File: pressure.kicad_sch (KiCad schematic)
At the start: 9 parts, among them IC1 HSFPAR004A, U6 INA317IDGKR

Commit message: finish up routing and fix latching
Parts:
- R21, R27: footprint Resistor_SMD:R_0603_1608Metric -> Resistor_SMD:R_1206_3216Metric
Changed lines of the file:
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@@
 			)
 		)
-		(property "Footprint" "Resistor_SMD:R_0603_1608Metric"
+		(property "Footprint" "Resistor_SMD:R_1206_3216Metric"
 			(at 110.998 63.5 90)
 			(effects
@@
 			)
 		)
-		(property "Footprint" "Resistor_SMD:R_0603_1608Metric"
+		(property "Footprint" "Resistor_SMD:R_1206_3216Metric"
 			(at 88.392 76.2 90)
 			(effects

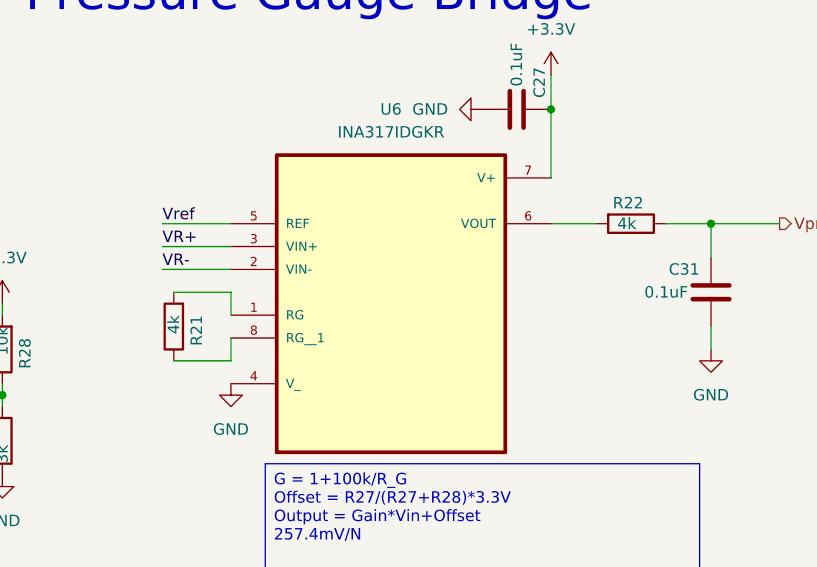
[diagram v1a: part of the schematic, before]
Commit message: replace some components for JLC order
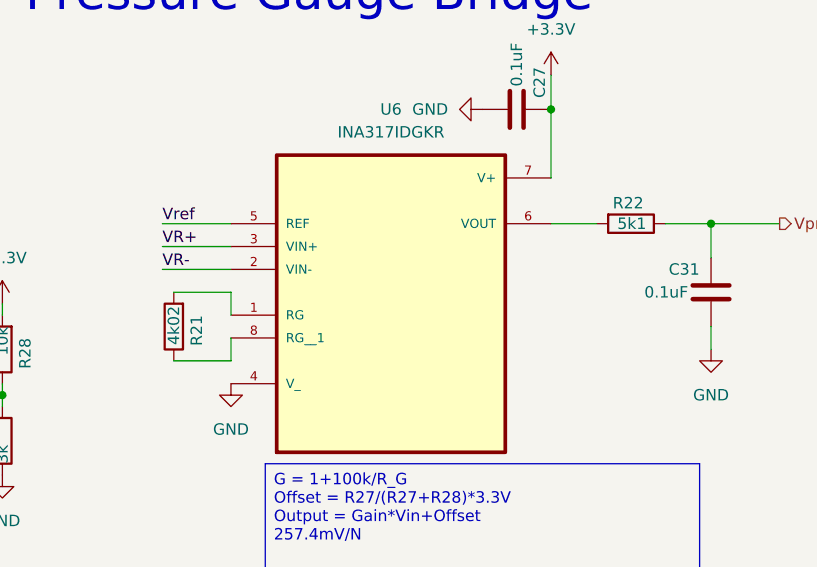
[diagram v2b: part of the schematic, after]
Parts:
- IC1: mpn (none) -> HSFPAR004A
- R21: value 4k -> 4k02; mpn CR0805-FX-1002ELF -> RC1206FR-074K02L
- R22: value 4k -> 5k1; mpn CR0805-FX-1002ELF -> (none)
- R27, R28: mpn CR0805-FX-1002ELF -> (none)
- U6: mpn (none) -> INA317IDGKR
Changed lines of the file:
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@@
 			)
 		)
-		(property "Value" "4k"
-			(at 109.22 62.23 90)
+		(property "Value" "4k02"
+			(at 109.22 61.214 90)
 			(effects
 				(font
@@
 			)
 		)
-		(property "mpn" "CR0805-FX-1002ELF "
+		(property "mpn" "RC1206FR-074K02L"
 			(at 109.22 63.5 0)
 			(effects
@@
 			)
 		)
-		(property "mpn" "CR0805-FX-1002ELF "
+		(property "mpn" ""
 			(at 90.17 76.2 0)
 			(effects
@@
 			)
 		)
+		(property "mpn" "INA317IDGKR"
+			(at 133.35 59.69 0)
+			(effects
+				(font
+					(size 1.27 1.27)
+				)
+				(hide yes)
+			)
+		)
 		(pin "6"
 		)
@@
 			)
 		)
-		(property "Value" "4k"
+		(property "Value" "5k1"
 			(at 158.496 52.07 90)
 			(effects
@@
 			)
 		)
-		(property "mpn" "CR0805-FX-1002ELF "
+		(property "mpn" ""
 			(at 160.02 52.07 0)
 			(effects
@@
 			)
 		)
+		(property "mpn" "HSFPAR004A"
+			(at 49.53 43.18 0)
+			(effects
+				(font
+					(size 1.27 1.27)
+				)
+				(hide yes)
+			)
+		)
 		(pin "4"
 		)
@@
 			)
 		)
-		(property "mpn" "CR0805-FX-1002ELF "
+		(property "mpn" ""
 			(at 90.17 66.04 0)
 			(effects

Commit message: add info in license to PCB design
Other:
- title: (none) -> Bierdeckel
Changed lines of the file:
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@@
 	(generator_version "9.0")
 	(paper "A4")
+	(title_block
+		(title "Bierdeckel")
+		(rev "0.4")
+		(comment 1 "SPDX-License-Identifier: CERN-OHL-S-2.0")
+		(comment 2 "SPDX-FileCopyrightText: 2023-2025 Stefan Riesenberger <stefan.riesenberger@gmail.com>")
+	)
 	(rectangle
 		(start 25.4 20.32)
